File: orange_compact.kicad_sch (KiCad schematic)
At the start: 225 parts, among them IC4 MAX13487EESA+T, J1 Battery, J4 Conn_Coaxial, J4 USB_B_Micro, J6 USB_B_Micro, J7 Conn_01x11_Pin, Q12 Q_NPN_BEC_BRT, Q2 MMBT3904, Q2 Q_NPN_BEC_BRT, Q3 MMBT3904, Q5 Q_NPN_BEC_BRT, Q6 Q_NPN_BEC_BRT, Q8 Q_NPN_BEC_BRT, SW1 SW_Push, SW2 SW_Push, U1 EG916QGLLG-N03-SGNSA, U10 LP5907MFX-3.3, U13 LIS2DH12TR, U14 LP5907MFX-1.8, U15 LM66100DCKR, U16 LM66100DCKR, U18 TPS61022, U19 LTV-217, U20 TPS566242DRLR, U22 TP4056, U25 ESP32-S3-MINI-1, U26 MCP2562-E/MF, U27 LP5907MFX-3.3, U28 USBLC6-2SC6, U29 TXB0108RGY, U30 TXB0104RUT, U5 LTV-217, U6 LMR14030SDDAR, U7 LP5907MFX-3.3, U8 1NCE IoT SIMs Chip, U9 USBLC6-2SC6

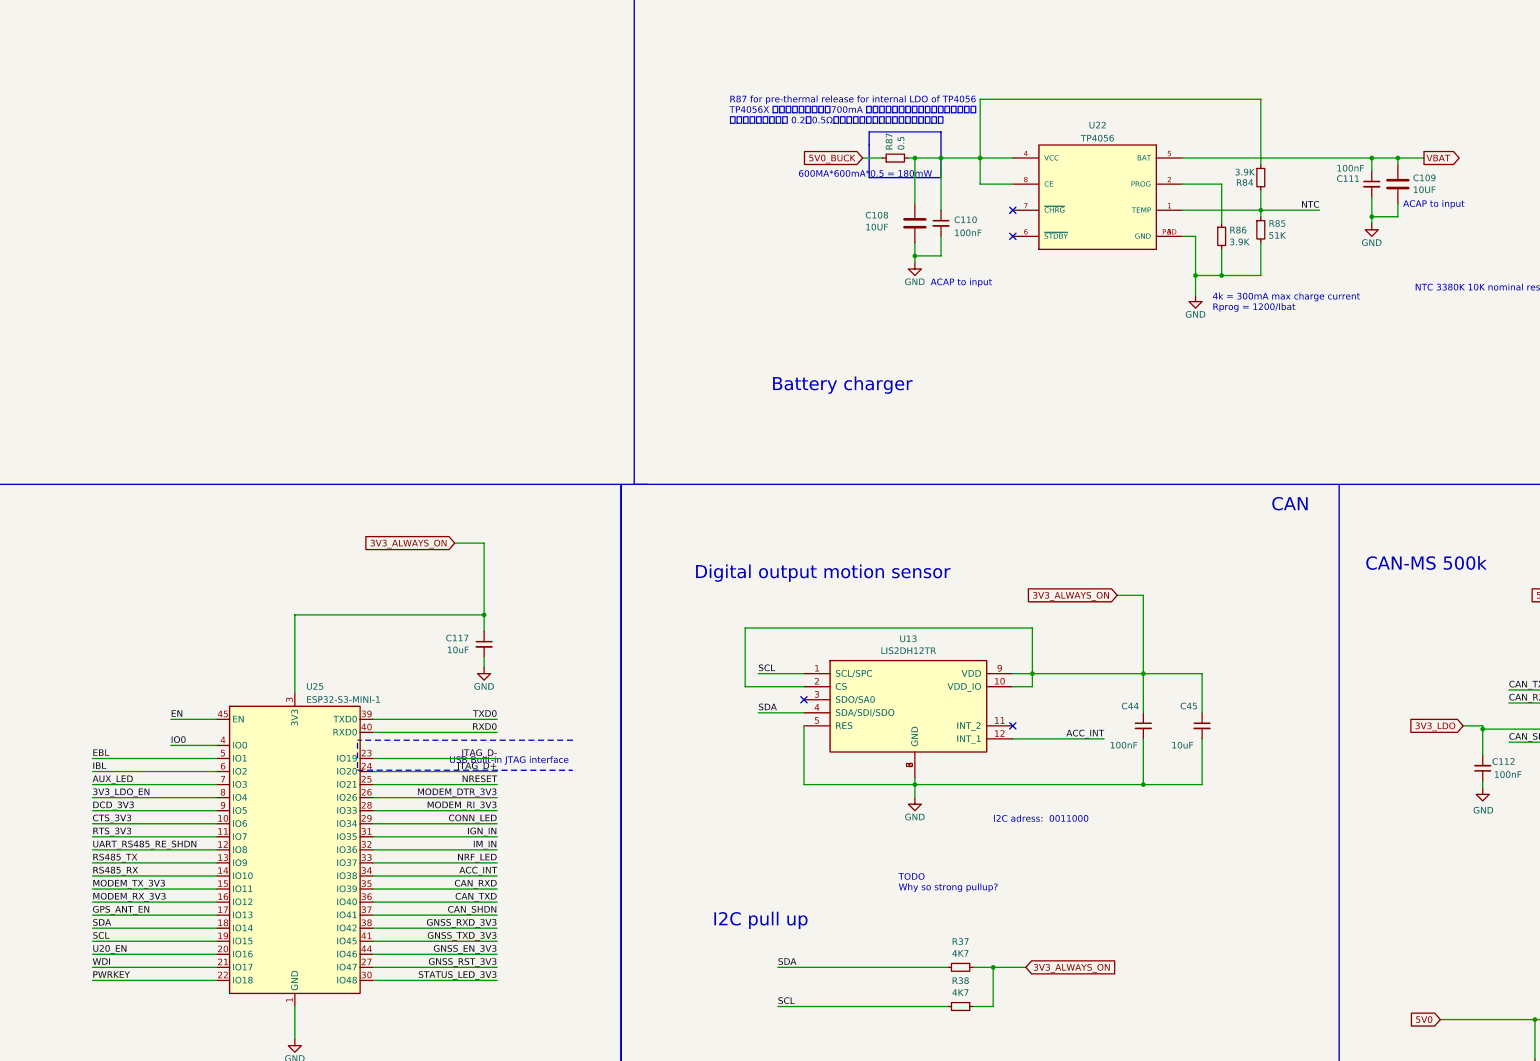
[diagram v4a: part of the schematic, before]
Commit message: added charge_enable
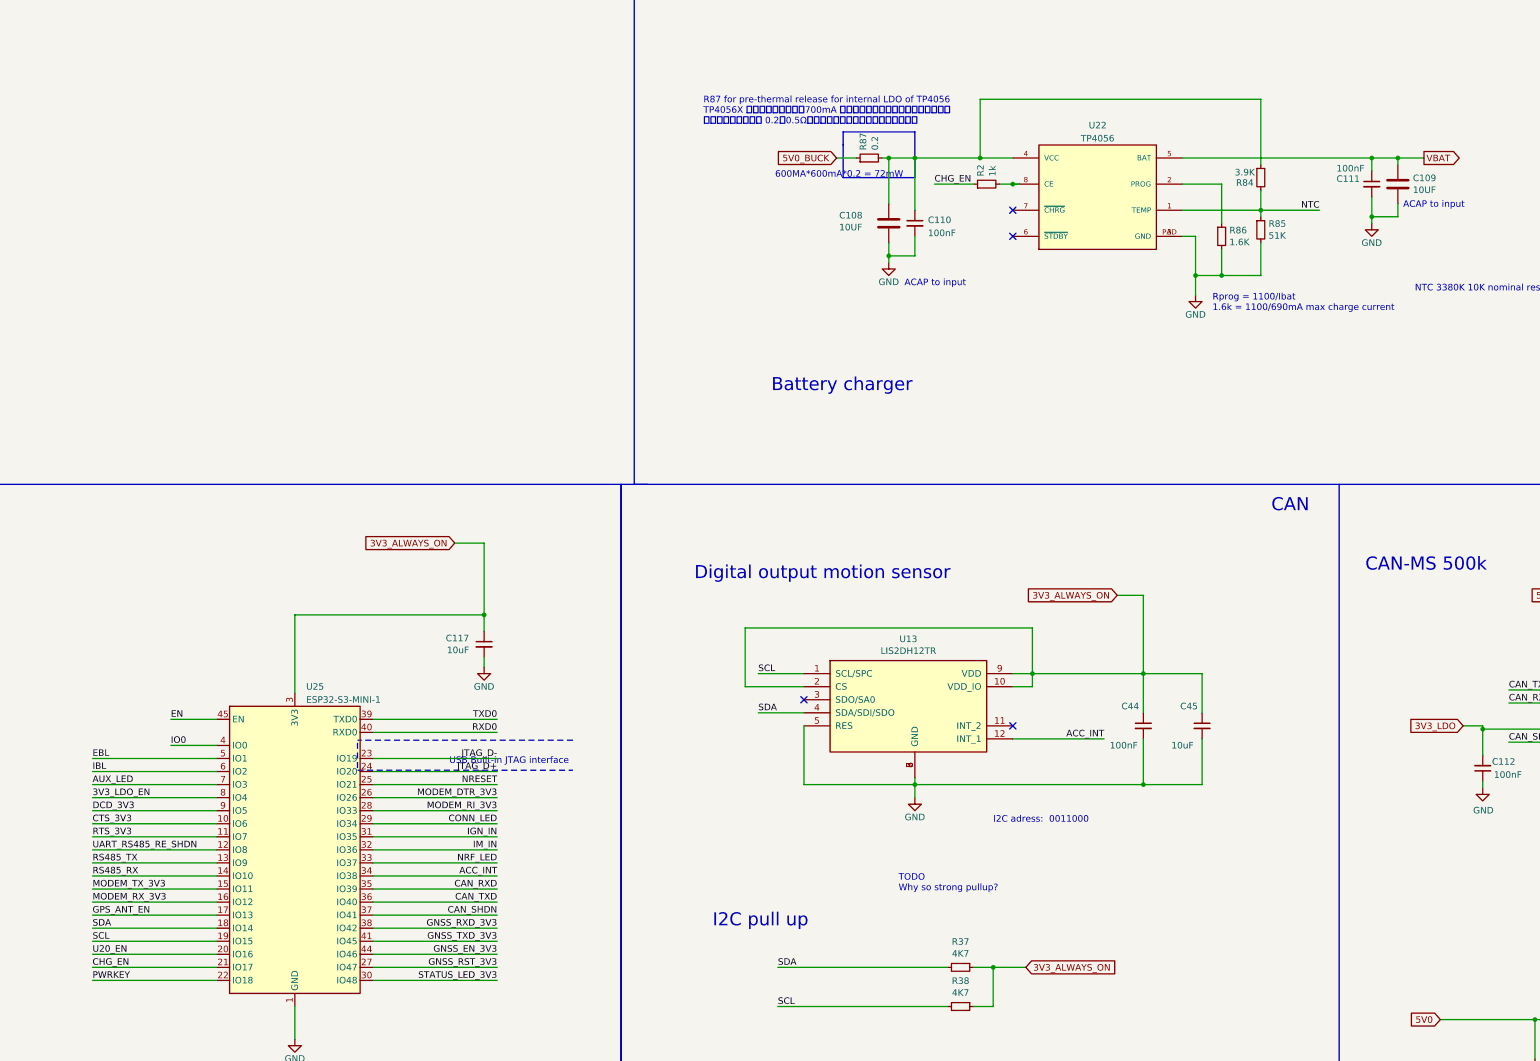
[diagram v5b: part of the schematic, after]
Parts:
- added R2: 1k, Resistor_SMD:R_0402_1005Metric, symbol Device:R_Small
- R86: value 3.9K -> 1.6K
- R87: value 0.5 -> 0.2; footprint Resistor_SMD:R_0603_1608Metric -> Resistor_SMD:R_0805_2012Metric
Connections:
- net at C108.1, C110.1, R84.1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: no longer U22.8 (CE)
- net WDI renamed CHG_EN
- net CHG_EN: now also R2.1
- new net: R2.2, U22.8 (CE)
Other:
- note added: "600MA*600mA*0.2 = 72mW"
- note added: "Rprog = 1100/Ibat 1.6k = 1100/690mA max charge current"
- note removed: "4k = 300mA max charge current Rprog = 1200/Ibat"
- note removed: "600MA*600mA*0.5 = 180mW"
- moved on the sheet: C108, C110, R87

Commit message: delete buttons capacitor
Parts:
- removed C69, C70: 0.1uF, Capacitor_SMD:C_0402_1005Metric, symbol Device:C
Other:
- moved on the sheet: C11, C24, C46, C47, C57, C76, D9, L7, R15, R22, R27, R28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

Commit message: added the level shifter for rs485
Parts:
- removed Q2, Q3: MMBT3904, Package_TO_SOT_SMD:SOT-23, symbol Transistor_BJT:MMBT3904
- removed R58, R59: 10k, Resistor_SMD:R_0402_1005Metric, symbol Device:R_Small
- removed R60, R61: 1k, Resistor_SMD:R_0402_1005Metric, symbol Device:R_Small
- added C1, C5: 100nF, Capacitor_SMD:C_0402_1005Metric, symbol Device:C_Small
- added R3, R6: 1k, Resistor_SMD:R_0402_1005Metric, symbol Device:R_Small
- added U2: TXB0102DCU, Package_SO:VSSOP-8_2.3x2mm_P0.5mm, symbol Logic_LevelTranslator:TXB0102DCU
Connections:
- net 3V3_LDO: now also C1.1, U2.3 (VCCA), U2.6 (OE)
- net 5V0: no longer C13.1, C14.1, IC4.8 (VCC), R32.2, R34.2, R35.2
- net 5V0_BUCK: now also C13.1, C14.1, IC4.8 (VCC), R32.2, R34.2, R35.2, C5.1, U2.7 (VCCB)
- net CAN_SHDN: now also R6.1; no longer U26.8 (SHDN)
- net GND: now also C1.2, C5.2, U2.2 (GND)
- net RS485_RX: now also U25.13 (IO9), U2.4 (A2); no longer U25.14 (IO10)
- net RS485_TX: now also U25.14 (IO10), U2.5 (A1); no longer U25.13 (IO9)
- net UART_RS485_RE_SHDN: no longer names the net of IC4.2 (~{RE}), IC4.3 (~{SHDN})
- net UART_RS485_RE_SHDN: now also R3.2; no longer U25.12 (IO8)
- net UART_RS485_RX_5V renamed RS485_TX_5V
- net RS485_TX_5V: now also U2.8 (B1)
- net UART_RS485_TX_5V renamed RS485_RX_5V
- net RS485_RX_5V: now also U2.1 (B2)
- new net: R6.2, U26.8 (SHDN)
- new net RS485_EN: R3.1, U25.12 (IO8)
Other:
- note added: "RS485 input voltage is 4.75 which hits the edge of internal battery booster's output, so route it to 5v_buck to enhance the stability Then RS485 can only operate with external power"
- moved on the sheet: C112, C14, C15, R13, U29

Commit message: changed GNSS level shifter to TXB0104PW(BIGGER)
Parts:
- removed U30: TXB0104RUT, Package_DFN_QFN:Texas_R-PUQFN-N12, symbol Logic_LevelTranslator:TXB0104RUT
- added U3: TXB0104PW, Package_SO:TSSOP-14_4.4x5mm_P0.65mm, symbol Logic_LevelTranslator:TXB0104PW
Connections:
- net +1V8: now also U3.1 (VCCA), U3.8 (OE)
- net 3V3_ALWAYS_ON: now also U3.14 (VCCB)
- net GND: now also U3.7 (GND)
- net GNSS_EN_1V8: now also U3.2 (A1)
- net GNSS_EN_3V3: now also U3.13 (B1)
- net GNSS_RST_1V8: now also U3.3 (A2)
- net GNSS_RST_3V3: now also U3.12 (B2)
- net GNSS_RXD_1V8: now also U3.5 (A4)
- net GNSS_RXD_3V3: now also U3.10 (B4)
- net GNSS_TXD_1V8: now also U3.4 (A3)
- net GNSS_TXD_3V3: now also U3.11 (B3)
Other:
- moved on the sheet: C1, C5, U2
